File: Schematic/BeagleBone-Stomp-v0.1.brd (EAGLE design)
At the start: 100 x 80 mm, 53 parts, among them U1 MSP430G2553_RHB_32, U2 TLV320AIC3120_RHB_32, U3 TPS73701_DRB_8

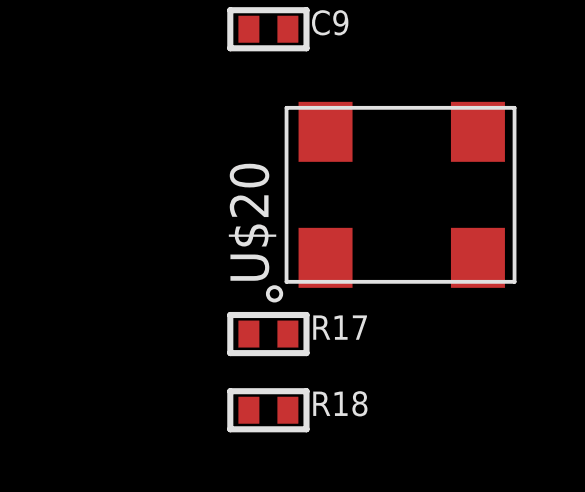
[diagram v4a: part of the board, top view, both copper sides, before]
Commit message: Adding in EEPROM chip
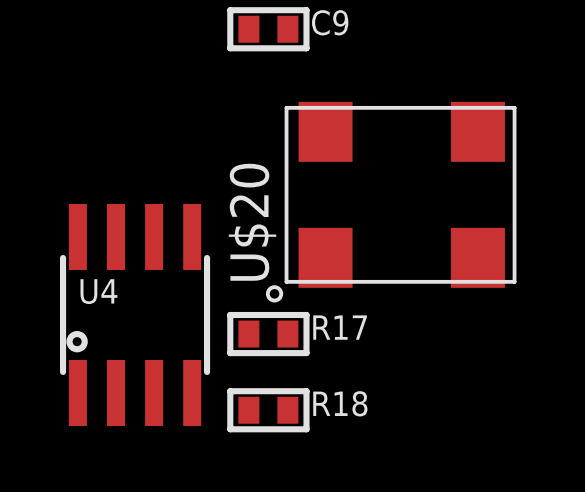
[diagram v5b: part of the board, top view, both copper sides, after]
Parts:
- added U4: (no value), microbuilder:SOIC8_150MIL
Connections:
- new net VCC: U4.8
- net GND: now also U4.4
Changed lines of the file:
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@@
 <element name="R17" library="microbuilder" package="0402" value="4.7k" x="1.905" y="-139.065"/>
 <element name="R18" library="microbuilder" package="0402" value="4.7k" x="1.905" y="-141.605"/>
+<element name="U4" library="microbuilder" package="SOIC8_150MIL" value="" x="-2.54" y="-138.43"/>
 </elements>
 <signals>
@@
 <contactref element="C9" pad="2"/>
 <contactref element="U$20" pad="GND"/>
-<wire x1="74.93" y1="61.595" x2="74.93" y2="64.135" width="0" layer="19" extent="1-1"/>
-<wire x1="45.0088" y1="45.7454" x2="74.93" y2="61.595" width="0" layer="19" extent="1-1"/>
-<wire x1="40.0812" y1="48.7426" x2="45.0088" y2="45.7454" width="0" layer="19" extent="1-1"/>
-<wire x1="39.1668" y1="54.9148" x2="40.0812" y2="48.7426" width="0" layer="19" extent="1-1"/>
-<wire x1="40.64" y1="55.88" x2="39.1668" y2="54.9148" width="0" layer="19" extent="1-1"/>
-<wire x1="40.0812" y1="36.449" x2="45.0088" y2="45.7454" width="0" layer="19" extent="1-1"/>
-<wire x1="40.64" y1="19.05" x2="40.0812" y2="36.449" width="0" layer="19" extent="1-1"/>
+<contactref element="U4" pad="4"/>
+<wire x1="8.89" y1="-136.525" x2="-0.635" y2="-141.03" width="0" layer="19" extent="1-1"/>
+<wire x1="2.555" y1="-128.905" x2="8.89" y2="-136.525" width="0" layer="19" extent="1-1"/>
+<wire x1="2.855" y1="-113.665" x2="2.555" y2="-128.905" width="0" layer="19" extent="1-1"/>
+<wire x1="2.855" y1="-111.125" x2="2.855" y2="-113.665" width="0" layer="19" extent="1-1"/>
+<wire x1="1.905" y1="-83.185" x2="2.855" y2="-111.125" width="0" layer="19" extent="1-1"/>
+<wire x1="2.555" y1="-47.625" x2="1.905" y2="-83.185" width="0" layer="19" extent="1-1"/>
+<wire x1="2.555" y1="-24.765" x2="2.555" y2="-47.625" width="0" layer="19" extent="1-1"/>
+<wire x1="2.413" y1="-22.225" x2="2.555" y2="-24.765" width="0" layer="19" extent="1-1"/>
+<wire x1="1.255" y1="-16.51" x2="2.413" y2="-22.225" width="0" layer="19" extent="1-1"/>
+<wire x1="2.555" y1="-1.27" x2="1.255" y2="-16.51" width="0" layer="19" extent="1-1"/>
+<wire x1="40.64" y1="19.05" x2="2.555" y2="-1.27" width="0" layer="19" extent="1-1"/>
 <wire x1="43.18" y1="19.05" x2="40.64" y2="19.05" width="0" layer="19" extent="1-1"/>
 <wire x1="45.72" y1="19.05" x2="43.18" y2="19.05" width="0" layer="19" extent="1-1"/>
@@
 <wire x1="74.93" y1="15.875" x2="71.12" y2="19.05" width="0" layer="19" extent="1-1"/>
 <wire x1="74.93" y1="13.335" x2="74.93" y2="15.875" width="0" layer="19" extent="1-1"/>
+<wire x1="40.0812" y1="36.449" x2="40.64" y2="19.05" width="0" layer="19" extent="1-1"/>
+<wire x1="45.0088" y1="45.7454" x2="40.0812" y2="36.449" width="0" layer="19" extent="1-1"/>
+<wire x1="40.0812" y1="48.7426" x2="45.0088" y2="45.7454" width="0" layer="19" extent="1-1"/>
+<wire x1="39.1668" y1="54.9148" x2="40.0812" y2="48.7426" width="0" layer="19" extent="1-1"/>
+<wire x1="40.64" y1="55.88" x2="39.1668" y2="54.9148" width="0" layer="19" extent="1-1"/>
 <wire x1="21.59" y1="61.595" x2="39.1668" y2="54.9148" width="0" layer="19" extent="1-1"/>
 <wire x1="21.59" y1="64.135" x2="21.59" y2="61.595" width="0" layer="19" extent="1-1"/>
 <wire x1="19.05" y1="64.135" x2="21.59" y2="64.135" width="0" layer="19" extent="1-1"/>
 <wire x1="19.05" y1="61.595" x2="21.59" y2="61.595" width="0" layer="19" extent="1-1"/>
-<wire x1="2.555" y1="-1.27" x2="40.64" y2="19.05" width="0" layer="19" extent="1-1"/>
-<wire x1="1.255" y1="-16.51" x2="2.555" y2="-1.27" width="0" layer="19" extent="1-1"/>
-<wire x1="2.413" y1="-22.225" x2="1.255" y2="-16.51" width="0" layer="19" extent="1-1"/>
-<wire x1="2.555" y1="-24.765" x2="2.413" y2="-22.225" width="0" layer="19" extent="1-1"/>
-<wire x1="2.555" y1="-47.625" x2="2.555" y2="-24.765" width="0" layer="19" extent="1-1"/>
-<wire x1="1.905" y1="-83.185" x2="2.555" y2="-47.625" width="0" layer="19" extent="1-1"/>
-<wire x1="2.855" y1="-111.125" x2="1.905" y2="-83.185" width="0" layer="19" extent="1-1"/>
-<wire x1="2.855" y1="-113.665" x2="2.855" y2="-111.125" width="0" layer="19" extent="1-1"/>
-<wire x1="2.555" y1="-128.905" x2="2.855" y2="-113.665" width="0" layer="19" extent="1-1"/>
-<wire x1="8.89" y1="-136.525" x2="2.555" y2="-128.905" width="0" layer="19" extent="1-1"/>
+<wire x1="74.93" y1="61.595" x2="45.0088" y2="45.7454" width="0" layer="19" extent="1-1"/>
+<wire x1="74.93" y1="64.135" x2="74.93" y2="61.595" width="0" layer="19" extent="1-1"/>
 </signal>
 <signal name="AVCC">
@@
 <wire x1="40.0812" y1="45.7454" x2="36.83" y2="64.135" width="0" layer="19" extent="1-1"/>
 </signal>
-<signal name="N$44">
-<contactref element="U$2" pad="66"/>
-<contactref element="U1" pad="22"/>
-<contactref element="U2" pad="9"/>
-<contactref element="R18" pad="1"/>
-<wire x1="41.783" y1="38.6588" x2="1.255" y2="-141.605" width="0" layer="19" extent="1-1"/>
-<wire x1="40.7924" y1="44.5262" x2="41.783" y2="38.6588" width="0" layer="19" extent="1-1"/>
-<wire x1="52.07" y1="61.595" x2="40.7924" y2="44.5262" width="0" layer="19" extent="1-1"/>
-</signal>
 <signal name="N$46">
 <contactref element="U2" pad="10"/>
@@
 <wire x1="41.3004" y1="49.4538" x2="64.77" y2="61.595" width="0" layer="19" extent="1-1"/>
 </signal>
+<signal name="VCC">
+<contactref element="U4" pad="8"/>
+</signal>
+<signal name="N$47">
+<contactref element="U2" pad="9"/>
+<contactref element="U$2" pad="66"/>
+<contactref element="U1" pad="22"/>
+<contactref element="R18" pad="1"/>
+<wire x1="41.783" y1="38.6588" x2="1.255" y2="-141.605" width="0" layer="19" extent="1-1"/>
+<wire x1="40.7924" y1="44.5262" x2="41.783" y2="38.6588" width="0" layer="19" extent="1-1"/>
+<wire x1="52.07" y1="61.595" x2="40.7924" y2="44.5262" width="0" layer="19" extent="1-1"/>
+</signal>
 </signals>

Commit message: Pretty close to being done just need to check connections on schematic and make BOM
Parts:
- removed C13: 0.1u, microbuilder:0402
- added C11: 0.1u, microbuilder:0402
- added R19, R20, R21: 4.7k, microbuilder:0402
- added R22: 10k, microbuilder:0402
- added SW1: (no value), microbuilder:DIPSWITCH_2PIN
- R3, R4, R5, R6, R7, R8, R9: value 470 -> 100
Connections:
- removed net AVCC: U$2.39
- removed net N$17: JP2.1, U1.5
- removed net N$19: JP2.4, U1.2
- removed net N$20: JP2.5, U1.1
- removed net N$21: JP2.3, U1.3
- removed net N$24: U$2.71, U2.5
- removed net N$25: JP1.19, U1.15
- removed net N$26: JP1.20, U1.14
- removed net N$27: JP1.14, U1.20
- removed net N$28: JP1.15, U1.19
- removed net N$29: JP1.16, U1.18
- removed net N$30: JP1.17, U1.17
- removed net N$31: JP1.18, U1.16
- removed net N$34: JP2.7, R16.2, U1.6
- removed net N$35: JP2.8, R15.2, U1.7
- removed net N$36: JP2.9, R14.2, U1.9
- removed net N$37: JP2.10, R13.2, U1.10
- removed net N$38: JP2.11, R12.2, U1.11
- removed net N$39: JP2.12, R11.2, U1.12
- removed net N$40: JP2.13, R10.2, U1.13
- removed net N$41: U$2.75, U2.6
- removed net N$42: U$2.77, U2.7
- removed net N$43: C16.1, C17.1, U2.21
- removed net N$45: U$2.56, U2.31
- removed net N$46: R17.1, U$2.65, U1.21, U2.10
- removed net N$47: R18.1, U$2.66, U1.22, U2.9
- removed net N$8 (its old number): U$20.OUT, U2.8
- removed net VCC: U4.8
- new net N$5: R19.1, SW1.1B, U4.1
- new net P$1: JP1.14, JP1.15, JP1.16, JP1.17, JP1.18, JP1.19, JP1.20, JP2.1, JP2.10, JP2.11, JP2.12, JP2.13, JP2.2, JP2.3, JP2.4, JP2.5, JP2.6, JP2.7, JP2.8, JP2.9, R10.2, R11.2, R12.2, R13.2, R14.2, R15.2, R16.2, R17.1, R18.1, U$1.SN, U$1.TN, U$2.56, U$2.65, U$2.66, U$2.71, U$2.74, U$2.75, U$2.77, U$20.E/D, U$20.OUT, U$7.SN, U$7.TN, U1.1, U1.10, U1.11, U1.12, U1.13, U1.14, U1.15, U1.16, U1.17, U1.18, U1.19, U1.2, U1.20, U1.21, U1.22, U1.25, U1.26, U1.3, U1.31, U1.32, U1.4, U1.5, U1.6, U1.7, U1.8, U1.9, U2.10, U2.11, U2.12, U2.13, U2.15, U2.30, U2.31, U2.32, U2.4, U2.5, U2.6, U2.7, U2.8, U2.9, U3.2, U3.6, U3.7, U4.5, U4.6
- net 3.3V: now also C11.1, R19.2, R20.2, R21.2, R22.2, U4.8; no longer C13.1
- net 5.0V: now also C16.1, C17.1, U2.21
- net AGND: no longer C13.2, U$2.38, U1.27, U1.33
- net GND: now also C11.2, SW1.1A, SW1.2A, U1.27, U1.33
- net N$11: now also R20.1, SW1.2B, U4.2; no longer U$2.74, U2.4
- net N$12: now also R21.1, U4.3; no longer JP2.6, U1.31
- net N$18: now also R22.1, U4.7; no longer JP2.2, U1.4

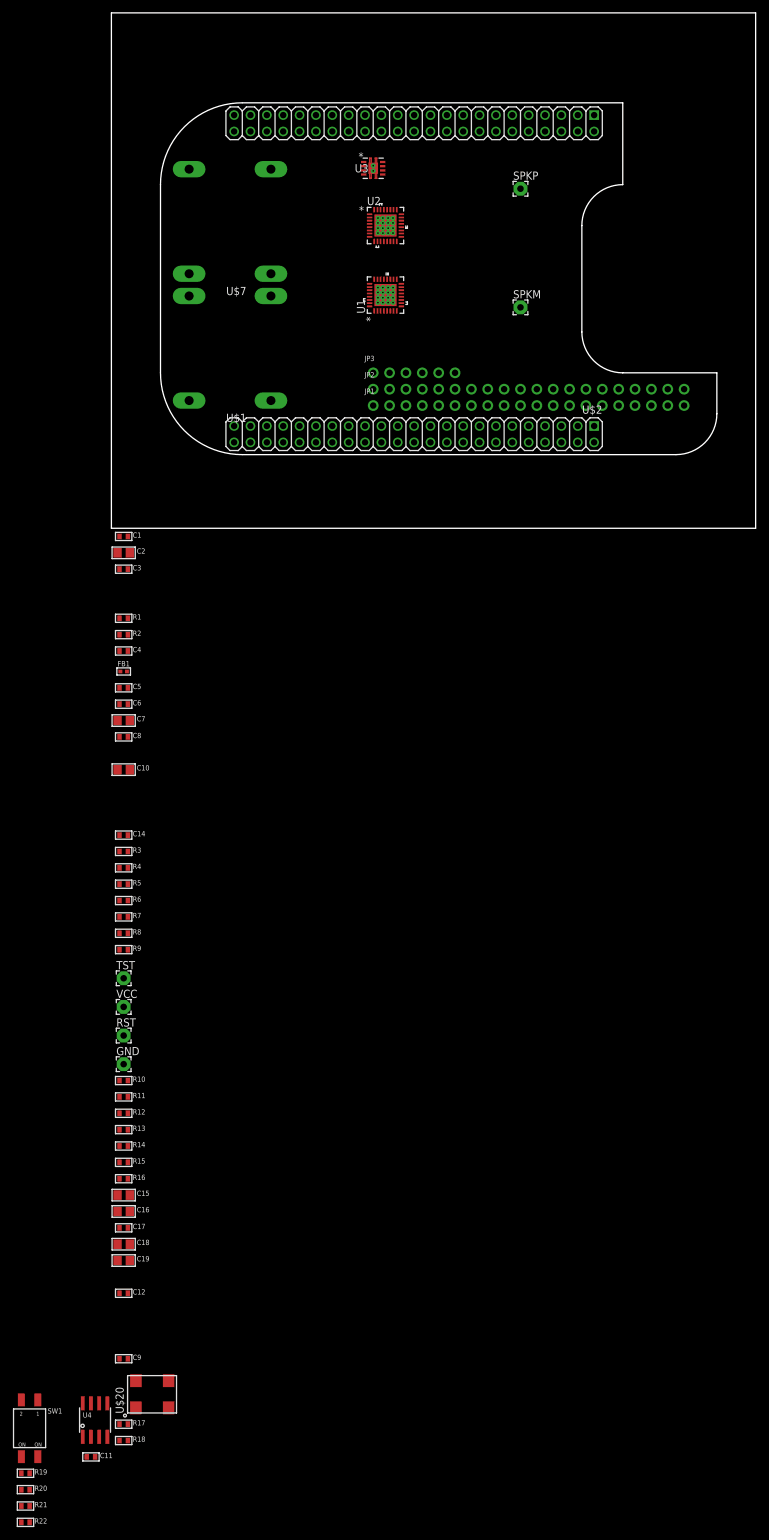
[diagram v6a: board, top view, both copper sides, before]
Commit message: Removing arrows and such
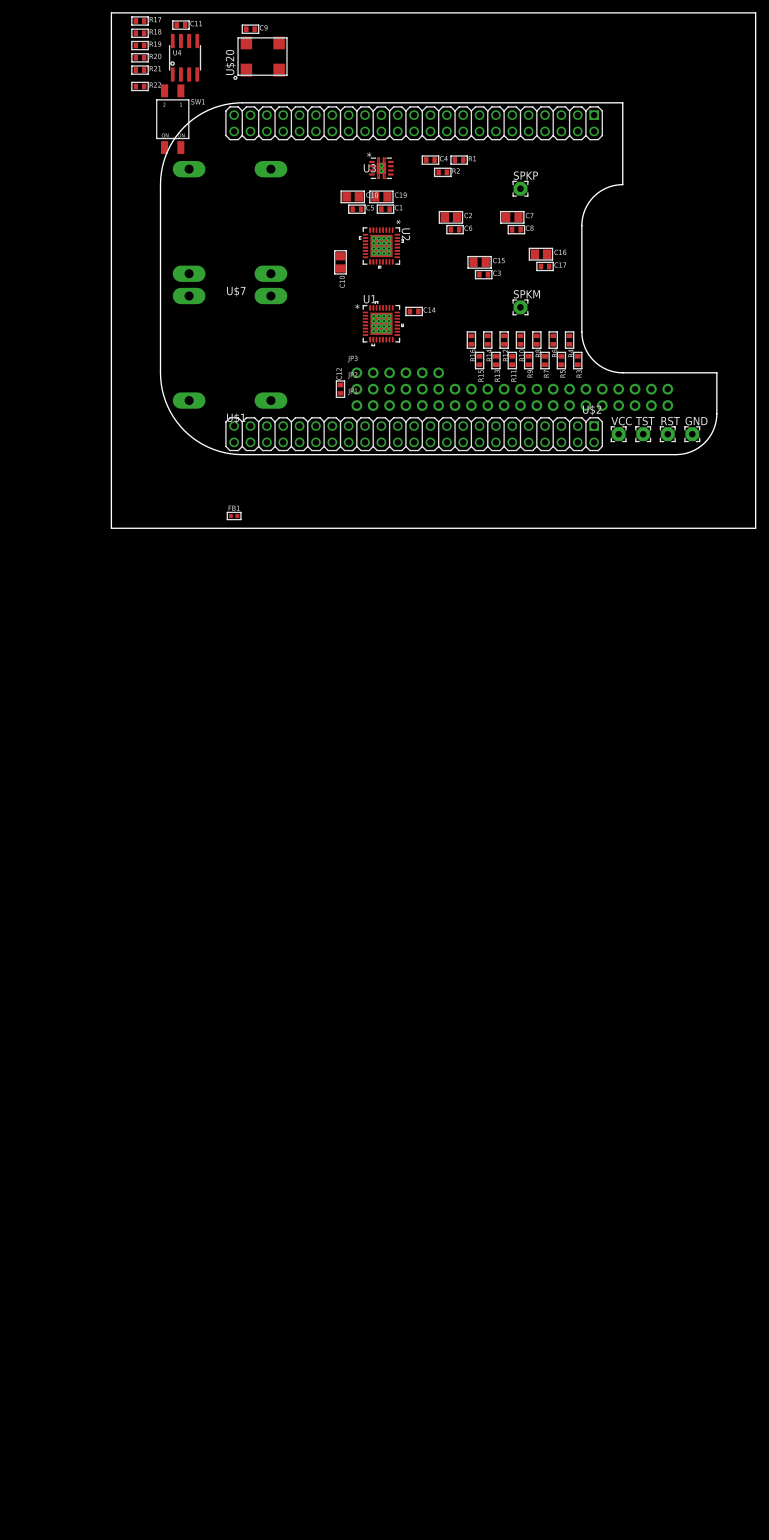
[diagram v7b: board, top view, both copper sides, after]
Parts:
- moved R21 223.6 mm to (4.45, 71.1)
- moved R22 223.6 mm to (4.45, 68.6)
- moved R20 223.0 mm to (4.45, 73.0)
- moved C11 222.7 mm to (10.8, 78.1)
- moved R19 222.3 mm to (4.45, 74.9)
- moved R18 218.5 mm to (4.45, 76.8)
- moved R17 217.8 mm to (4.45, 78.7)
- moved U4 211.9 mm to (11.4, 73.0)
- moved U$20 208.4 mm to (21.0, 71.1)
- moved C9 207.3 mm to (21.6, 77.5)
- moved SW1 204.4 mm to (9.53, 63.5)
- moved C19 169.9 mm to (41.9, 51.4)
- moved C18 166.4 mm to (37.5, 51.4)
- moved C17 162.9 mm to (67.3, 40.6)
- moved C16 162.1 mm to (66.7, 42.5)
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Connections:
- removed net P$1: JP1.14, JP1.15, JP1.16, JP1.17, JP1.18, JP1.19, JP1.20, JP2.1, JP2.10, JP2.11, JP2.12, JP2.13, JP2.2, JP2.3, JP2.4, JP2.5, JP2.6, JP2.7, JP2.8, JP2.9, R10.2, R11.2, R12.2, R13.2, R14.2, R15.2, R16.2, R17.1, R18.1, U$1.SN, U$1.TN, U$2.56, U$2.65, U$2.66, U$2.71, U$2.74, U$2.75, U$2.77, U$20.E/D, U$20.OUT, U$7.SN, U$7.TN, U1.1, U1.10, U1.11, U1.12, U1.13, U1.14, U1.15, U1.16, U1.17, U1.18, U1.19, U1.2, U1.20, U1.21, U1.22, U1.25, U1.26, U1.3, U1.31, U1.32, U1.4, U1.5, U1.6, U1.7, U1.8, U1.9, U2.10, U2.11, U2.12, U2.13, U2.15, U2.30, U2.31, U2.32, U2.4, U2.5, U2.6, U2.7, U2.8, U2.9, U3.2, U3.6, U3.7, U4.5, U4.6
- new net CODEC_BCLK: U$2.77, U2.7
- new net CODEC_DIN: U$2.71, U2.5
- new net CODEC_DOUT: U$2.74, U2.4
- new net CODEC_MCLK: U$20.OUT, U2.8
- new net CODEC_WCLK: U$2.75, U2.6
- new net I2C_CLK: R17.1, U$2.65, U1.21, U2.10, U4.6
- new net I2C_DATA: R18.1, U$2.66, U1.22, U2.9, U4.5
- new net LED1: JP1.14, U1.14
- new net LED2: JP1.15, U1.15
- new net LED3: JP1.16, U1.16
- new net LED4: JP1.17, U1.17
- new net LED5: JP1.18, U1.18
- new net LED6: JP1.19, U1.19
- new net LED7: JP1.20, U1.20
- new net POT1: JP2.1, U1.31
- new net POT2: JP2.2, U1.1
- new net POT3: JP2.3, U1.2
- new net POT4: JP2.4, U1.3
- new net POT5: JP2.5, U1.4
- new net POT6: JP2.6, U1.5
- new net RESET: U$2.56, U2.31
- new net STOMP1: JP2.7, R16.2, U1.6
- new net STOMP2: JP2.8, R15.2, U1.7
- new net STOMP3: JP2.9, R14.2, U1.9
- new net STOMP4: JP2.10, R13.2, U1.10
- new net STOMP5: JP2.11, R12.2, U1.11
- new net STOMP6: JP2.12, R11.2, U1.12
- new net STOMP7: JP2.13, R10.2, U1.13

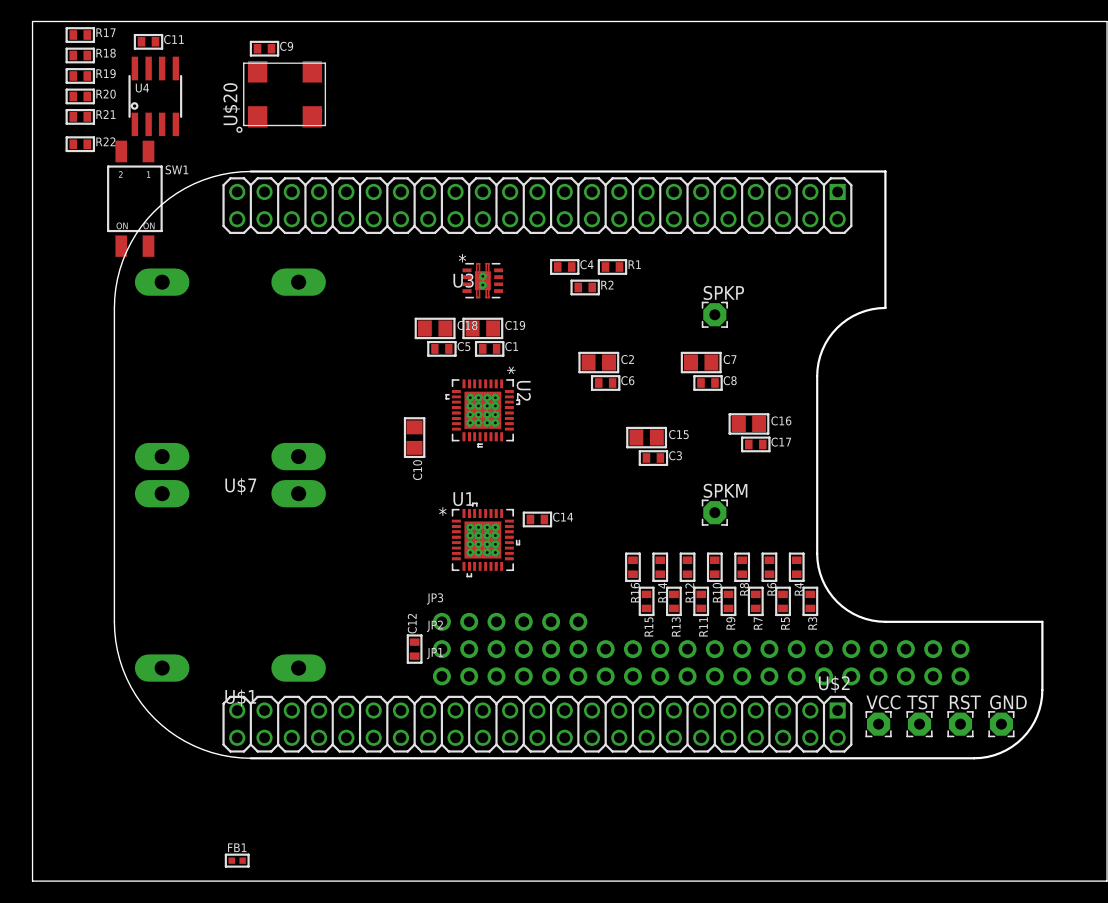
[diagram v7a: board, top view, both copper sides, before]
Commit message: Cleaning libraries up
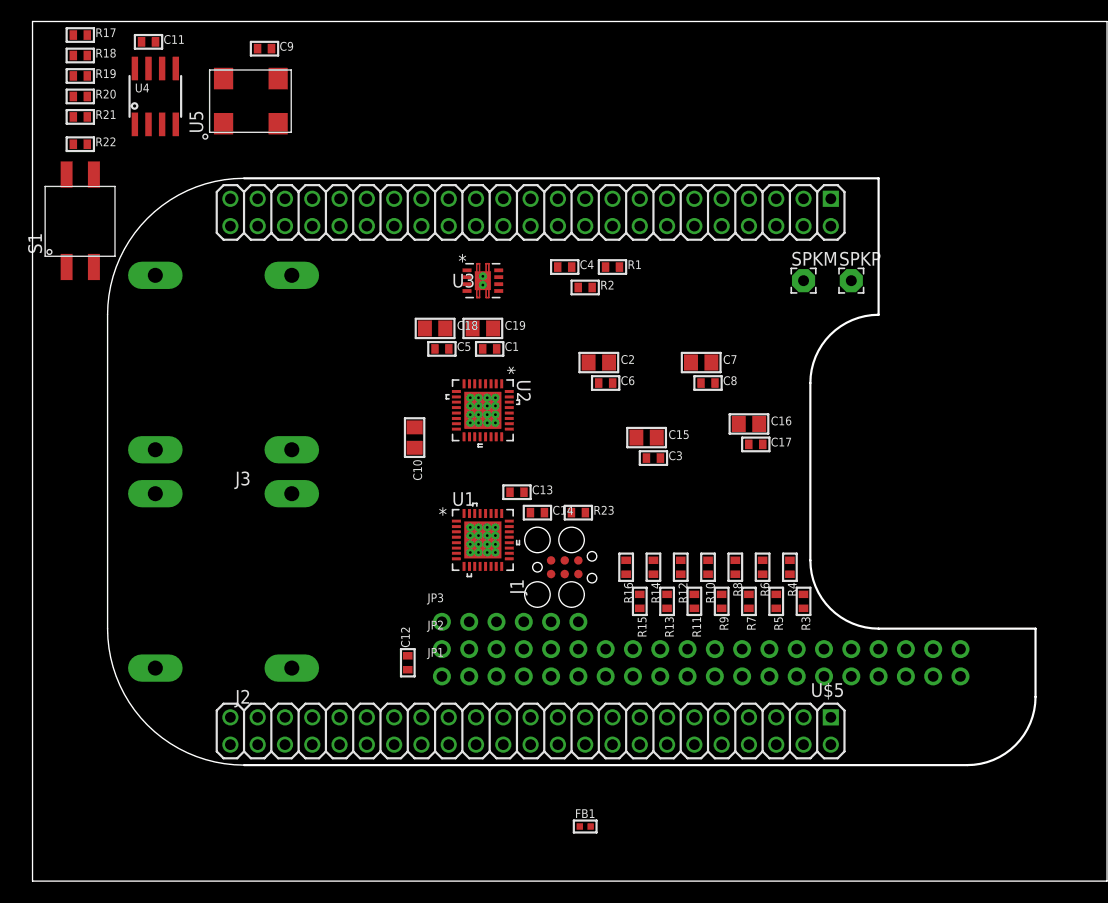
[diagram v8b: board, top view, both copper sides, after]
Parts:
- removed GND, RST, TST, VCC: WIREPAD2,15/1,0, wirepad:2,15/1,0
- removed SW1: (no value), microbuilder:DIPSWITCH_2PIN
- removed U$1, U$7: NMJ4HFD2, bone:NMJ4HFD2
- removed U$2: BEAGLEBONE_OUTLINE, microbuilder:BEAGLEBONE_SHIELD
- removed U$20: FXO-HC735-12, bone:FXO-HC735-12
- added C13: 2.2u, microbuilder:0402
- added J1: (no value), bone:TC2030-MCP
- added J2, J3: NMJ4HFD2, bone:NMJ4HFD2
- added R23: 47k, microbuilder:0402
- added S1: CTS-219-2MST, bone:CTS-219-2MST
- added U$5: BEAGLEBONE_OUTLINE, bone:BEAGLEBONE_SHIELD
- added U5: FXO-HC735-12, bone:FXO-HC735-12
- moved FB1 32.5 mm to (51.4, 5.08)
- moved SPKM 23.1 mm to (71.8, 55.9)
- moved SPKP 13.1 mm to (76.2, 55.9)
- moved C12 1.42 mm to (34.9, 20.3)
- moved R14 0.64 mm to (57.8, 29.2)
- moved R16 0.64 mm to (55.2, 29.2)
- moved R3 0.64 mm to (71.8, 26.0)
- moved R4 0.64 mm to (70.5, 29.2)
- moved R6 0.64 mm to (67.9, 29.2)
- moved R7 0.64 mm to (66.7, 26.0)
- moved R8 0.64 mm to (65.4, 29.2)
- moved C14 0.63 mm to (47.0, 34.3)
- moved R10 0.63 mm to (62.9, 29.2)
- moved R11 0.63 mm to (61.6, 26.0)
- moved R12 0.63 mm to (60.3, 29.2)
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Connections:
- new net TCK: J1.3
- new net VCC_OUT: J1.2
- net 3.3V: now also J1.4, R23.2, U$5.49, U$5.50, U5.VDD; no longer U$2.49, U$2.50, U$20.VDD, VCC.1
- net 5.0V: now also U$5.53, U$5.54; no longer U$2.53, U$2.54
- net AGND: now also J2.S, J3.S; no longer U$1.S, U$7.S
- net CODEC_BCLK: now also U$5.77; no longer U$2.77
- net CODEC_DIN: now also U$5.71; no longer U$2.71
- net CODEC_DOUT: now also U$5.74; no longer U$2.74
- net CODEC_MCLK: now also U5.OUT; no longer U$20.OUT
- net CODEC_WCLK: now also U$5.75; no longer U$2.75
- net GND: now also C13.2, J1.5, S1.P$1, S1.P$2, U$5.1, U$5.2, U$5.47, U$5.48, U$5.89, U$5.90, U$5.91, U$5.92, U5.GND; no longer GND.1, SW1.1A, SW1.2A, U$2.1, U$2.2, U$2.47, U$2.48, U$2.89, U$2.90, U$2.91, U$2.92, U$20.GND
- net GNDA_ADC: now also U$5.80; no longer U$2.80
- net I2C_CLK: now also U$5.65; no longer U$2.65
- net I2C_DATA: now also U$5.66; no longer U$2.66
- net N$11: now also S1.P$3; no longer SW1.2B
- net N$32: now also J1.6; no longer TST.1
- net N$33: now also C13.1, J1.1, R23.1; no longer RST.1
- net N$5: now also S1.P$4; no longer SW1.1B
- net N$6: now also J3.T; no longer U$7.T
- net N$9: now also J2.T; no longer U$1.T
- net RESET: now also U$5.56; no longer U$2.56
- net VDD_5V: now also U$5.51, U$5.52; no longer U$2.51, U$2.52
- net VDD_ADC: now also U$5.78; no longer U$2.78
